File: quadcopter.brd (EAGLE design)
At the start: 178 x 178 mm, 66 parts, among them J1 ISP, SW1 PUSHBUTTON_SMD-VERTICAL-1, U2 ATMEGA128RFA1

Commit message: moved net bridge and VREG closer to battery terminals
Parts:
- moved U$2 16.7 mm to (-10.8, 9.65)
- moved J4 13.8 mm to (-16.2, 6.93), turned to 45 degrees
- moved C27 12.1 mm to (-20.4, 4.00), turned to 90 degrees
- moved C28 7.41 mm to (-30.2, 4.05), turned to 90 degrees
- moved C13 4.60 mm to (-28.1, 5.80), turned to 270 degrees
- moved STEP_DOWN 4.08 mm to (-24.6, 4.80), turned to 90 degrees
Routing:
- net 3V: track 287.6 -> 142.7 mm, vias 5 -> 9
- net RX1: track 157.3 -> 119.0 mm
- net JUMPER_INPUT: track 22.2 -> 7.57 mm
- net SCL: track 99.5 -> 87.8 mm, vias 3 -> 1
- net BAT_GND: track 109.9 -> 98.4 mm, vias 6 -> 5
- net PE4: track 125.4 -> 136.0 mm, vias 2 -> 1
- net GND: track 226.0 -> 234.1 mm, vias 30 -> 29
- net VBAT: track 41.0 -> 47.2 mm, vias 8 -> 6
- net PE5: track 108.9 -> 103.0 mm

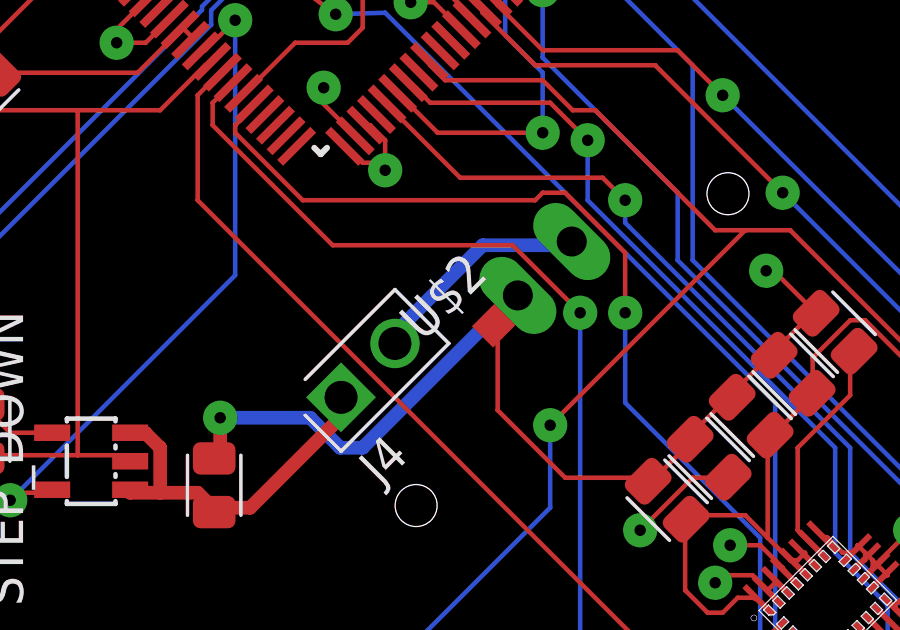
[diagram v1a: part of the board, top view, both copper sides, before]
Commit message: fixed drc things for closer net bridge
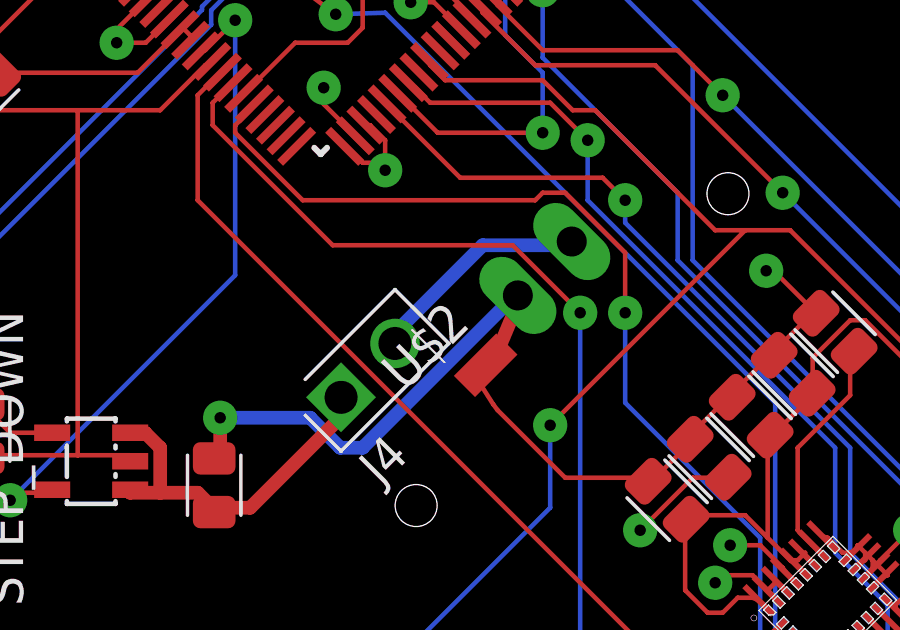
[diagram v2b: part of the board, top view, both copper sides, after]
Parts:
- moved U$2 1.76 mm to (-11.4, 8.00)
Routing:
- net BAT_GND: track 98.4 -> 100.1 mm
- net GND: track 234.1 -> 232.6 mm
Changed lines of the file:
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@@
 <attribute name="MPN" value="NA" x="-72.2" y="-0.7" size="1.778" layer="27" rot="R90" display="off"/>
 </element>
-<element name="U$2" library="quadparts_michael" package="NET_BRIDGE" value="NET_BRIDGE" x="-10.8" y="9.65" rot="R45">
-<attribute name="CREATOR" value="Michael" x="-10.8" y="9.65" size="1.778" layer="27" rot="R45" display="off"/>
-<attribute name="DIST" value="none" x="-10.8" y="9.65" size="1.778" layer="27" rot="R45" display="off"/>
-<attribute name="DISTPN" value="none" x="-10.8" y="9.65" size="1.778" layer="27" rot="R45" display="off"/>
-<attribute name="MFR" value="none" x="-10.8" y="9.65" size="1.778" layer="27" rot="R45" display="off"/>
-<attribute name="MPN" value="none" x="-10.8" y="9.65" size="1.778" layer="27" rot="R45" display="off"/>
-<attribute name="REVIEWER" value="group 4" x="-10.8" y="9.65" size="1.778" layer="27" rot="R45" display="off"/>
+<element name="U$2" library="quadparts_michael" package="NET_BRIDGE" value="NET_BRIDGE" x="-11.4" y="8" rot="R45">
+<attribute name="CREATOR" value="Michael" x="-11.4" y="8" size="1.778" layer="27" rot="R45" display="off"/>
+<attribute name="DIST" value="none" x="-11.4" y="8" size="1.778" layer="27" rot="R45" display="off"/>
+<attribute name="DISTPN" value="none" x="-11.4" y="8" size="1.778" layer="27" rot="R45" display="off"/>
+<attribute name="MFR" value="none" x="-11.4" y="8" size="1.778" layer="27" rot="R45" display="off"/>
+<attribute name="MPN" value="none" x="-11.4" y="8" size="1.778" layer="27" rot="R45" display="off"/>
+<attribute name="REVIEWER" value="group 4" x="-11.4" y="8" size="1.778" layer="27" rot="R45" display="off"/>
 </element>
 <element name="U$20" library="quadparts_michael" package="MOSFET" value="MOSFET-N_CHANNEL" x="-64.17" y="2.2">
@@
 <wire x1="-30" y1="5" x2="-30.2" y2="4.945" width="0.1524" layer="1"/>
 <wire x1="-28.25" y1="5" x2="-28.15" y2="4.905" width="0.1524" layer="1"/>
-<wire x1="-11" y1="6.5" x2="-11" y2="9.25" width="0.1524" layer="1"/>
+<wire x1="-11" y1="6.5" x2="-11.15" y2="6.7" width="0.1524" layer="1"/>
 <wire x1="-8.75" y1="4.25" x2="-11" y2="6.5" width="0.1524" layer="1"/>
 <wire x1="-6" y1="4.25" x2="-8.75" y2="4.25" width="0.1524" layer="1"/>
-<wire x1="-11" y1="9.25" x2="-11.153553125" y2="9.29644375" width="0.1524" layer="1"/>
+<wire x1="-11.15" y1="6.7" x2="-11.753553125" y2="7.64644375" width="0.1524" layer="1"/>
 <wire x1="-6" y1="4.25" x2="-5.982859375" y2="4.132859375" width="0.1524" layer="1"/>
 <wire x1="-22.25" y1="16.5" x2="-20.75" y2="18" width="0.1524" layer="1"/>
@@
 <wire x1="-20.25" y1="6.25" x2="-20.25" y2="5" width="0.4572" layer="1"/>
 <wire x1="-20.25" y1="5" x2="-20.45" y2="4.895" width="0.4572" layer="1"/>
-<wire x1="-10.25" y1="10.25" x2="-10.44644375" y2="10.003553125" width="0.4572" layer="1"/>
+<wire x1="-10.25" y1="10.25" x2="-11.04644375" y2="8.353553125" width="0.4572" layer="1"/>
 <wire x1="-10.25" y1="10.25" x2="-10.32729375" y2="10.32729375" width="0.4572" layer="1"/>
 <wire x1="-17.25" y1="6.25" x2="-20.25" y2="6.25" width="0.4572" layer="16"/>

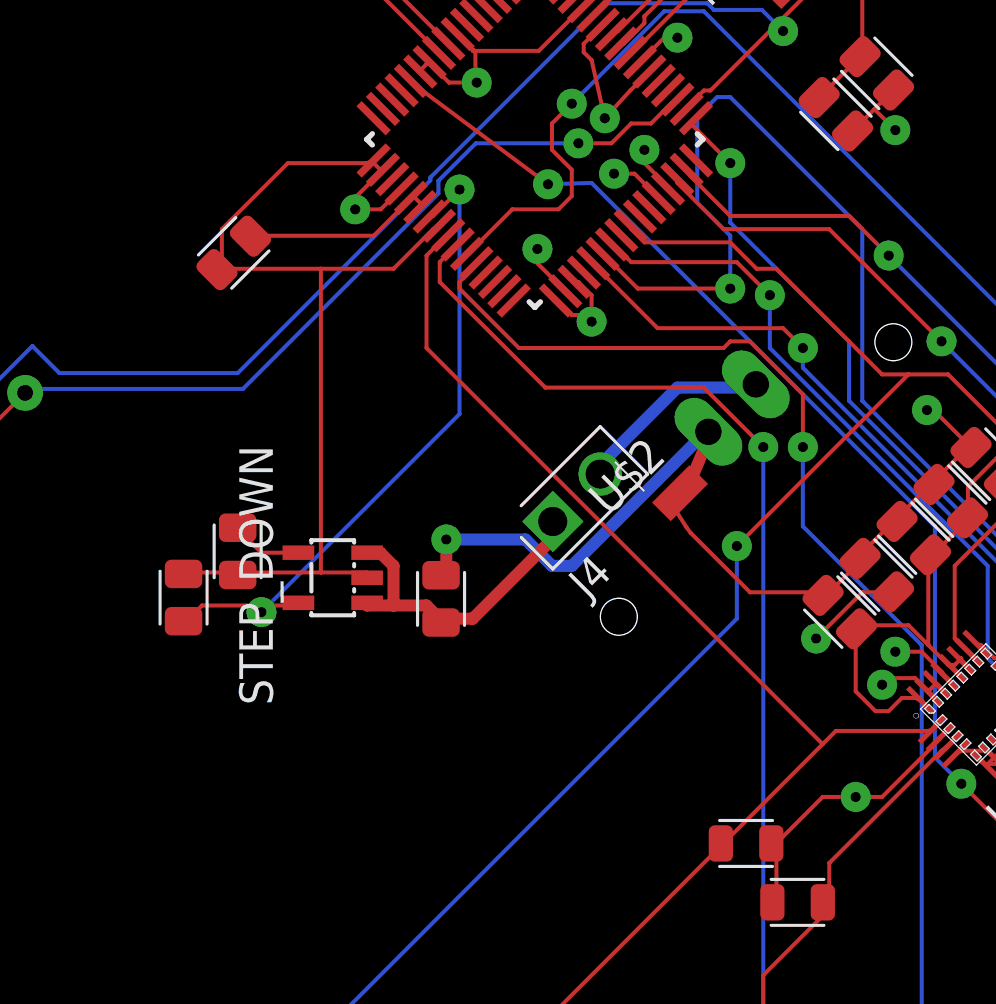
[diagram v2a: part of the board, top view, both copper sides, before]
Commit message: made vreg traces even shorter
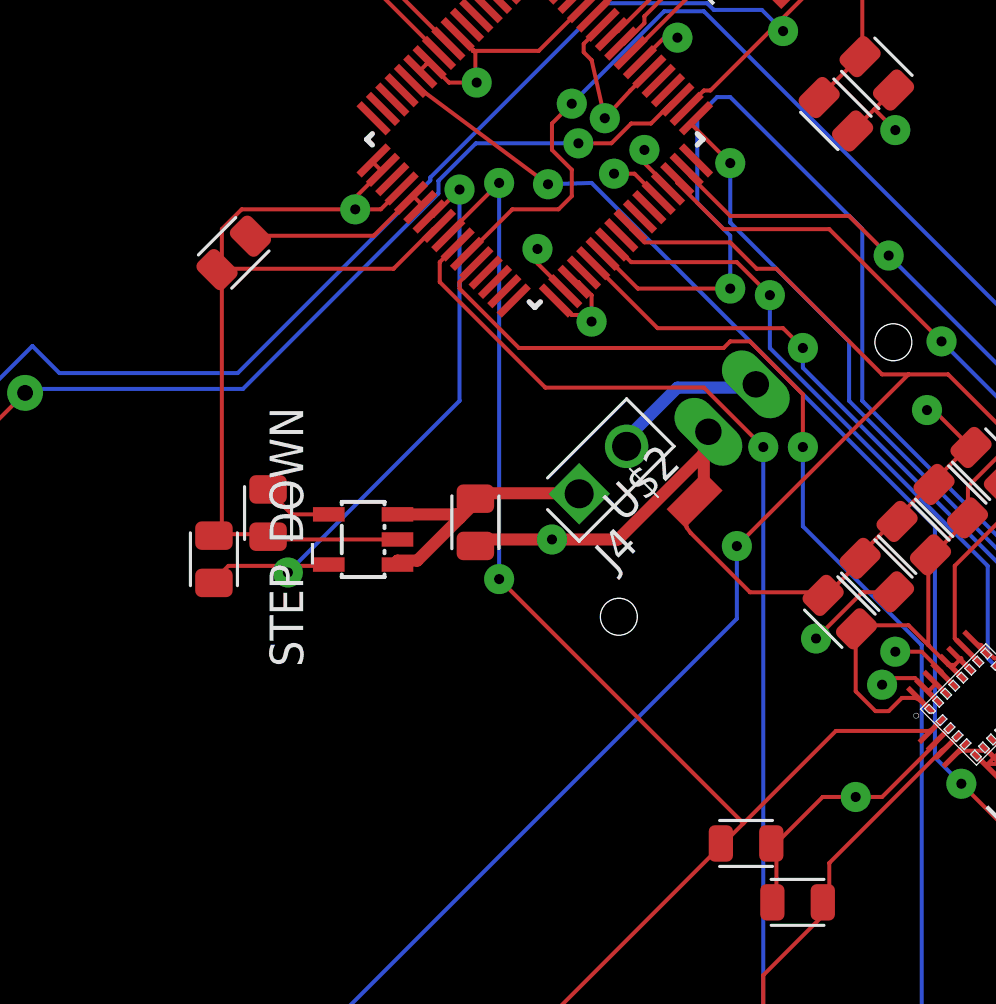
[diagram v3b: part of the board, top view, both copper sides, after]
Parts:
- moved C27 3.18 mm to (-19.1, 6.90), turned to 270 degrees
- moved STEP_DOWN 1.85 mm to (-23.4, 6.25)
- moved C13 1.85 mm to (-27.0, 7.25)
- moved C28 1.85 mm to (-29.1, 5.50)
- moved J4 1.45 mm to (-15.2, 7.98)
- moved U$2 0.60 mm to (-10.8, 7.75)
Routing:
- net SCL: track 87.8 -> 92.8 mm, vias 1 -> 3
- net GND: track 232.6 -> 229.4 mm
- net BAT_GND: track 100.1 -> 97.4 mm
- net 3V: track 142.7 -> 140.9 mm
- net JUMPER_INPUT: track 7.57 -> 6.07 mm
- net VBAT: track 47.2 -> 45.8 mm

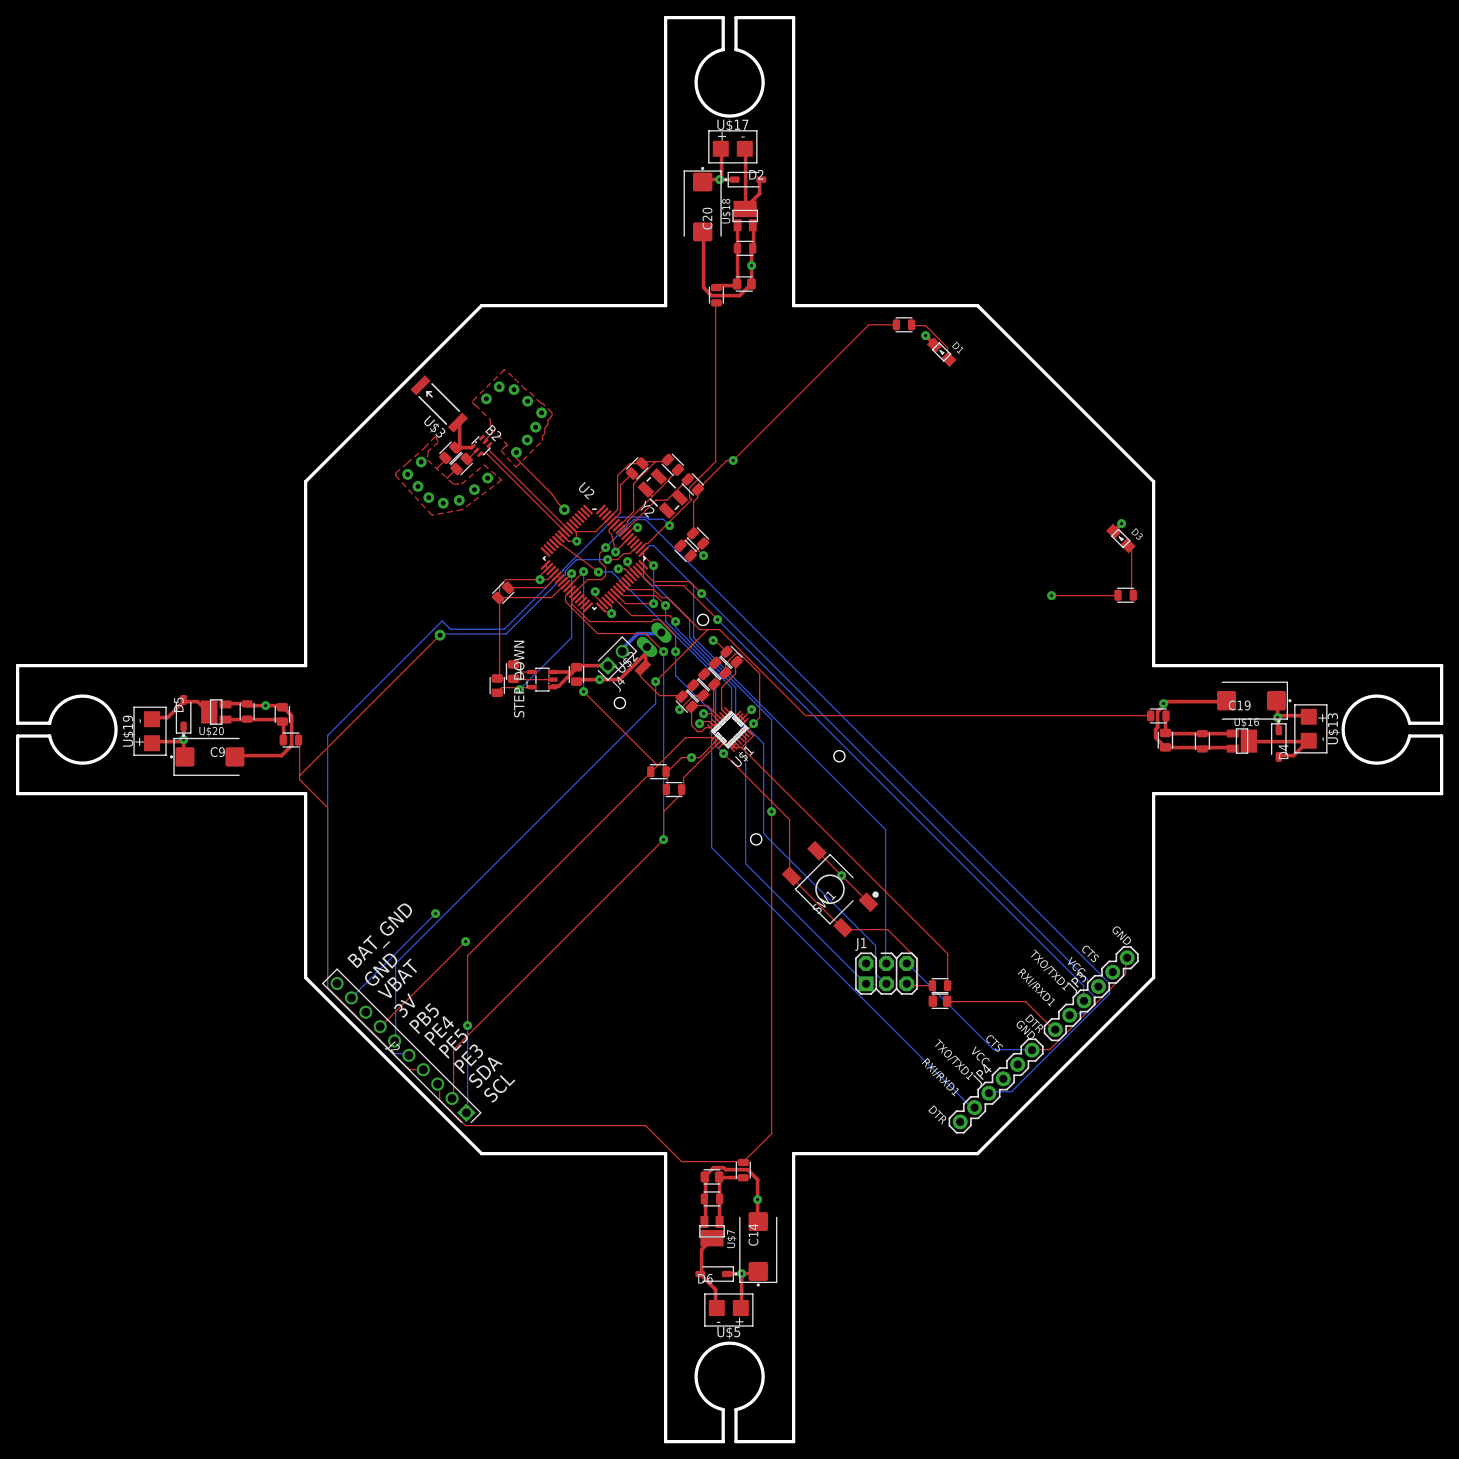
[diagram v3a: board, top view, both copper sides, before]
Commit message: rotated board to fit in box
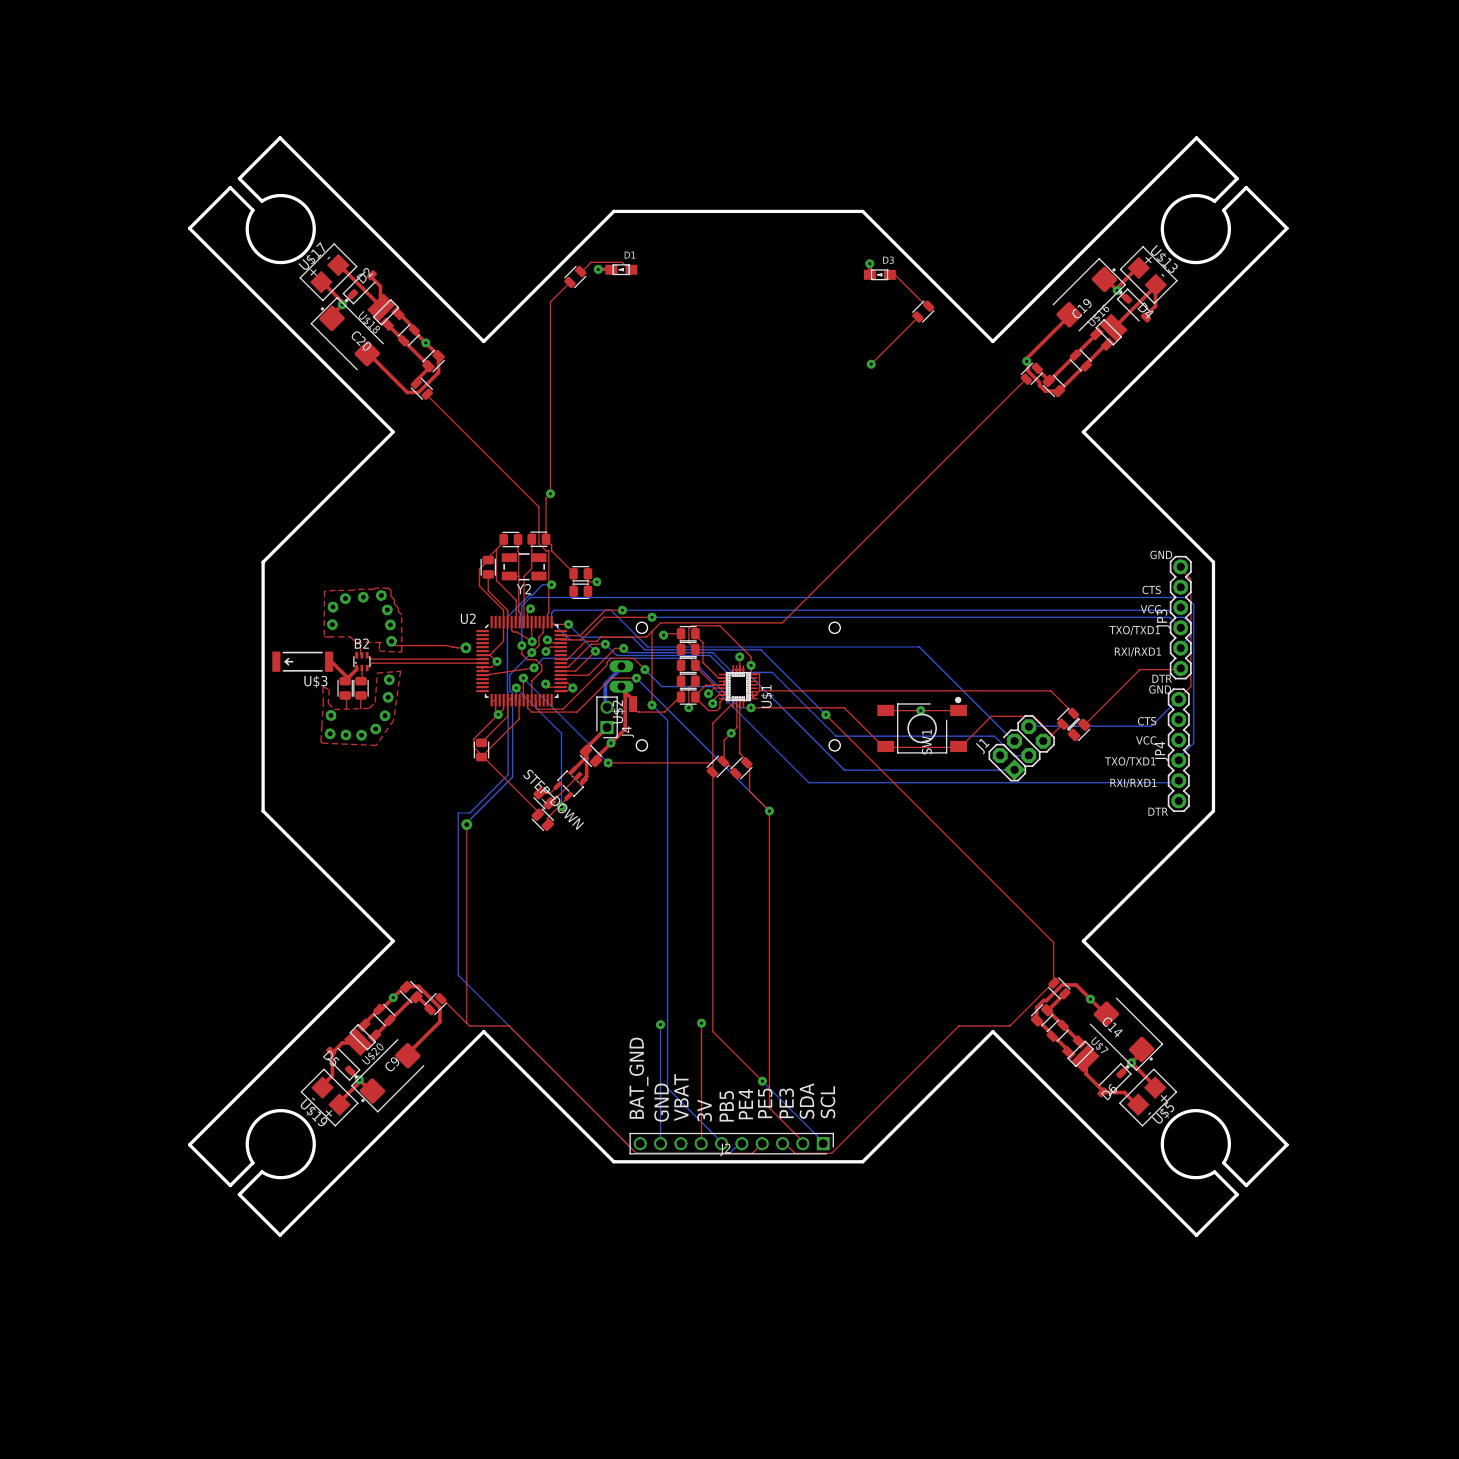
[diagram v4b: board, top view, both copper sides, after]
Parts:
- moved U$13 60.0 mm to (51.9, 57.0), turned to 315 degrees
- moved U$5 58.6 mm to (52.5, -45.5), turned to 225 degrees
- moved D4 57.3 mm to (50.9, 52.7), turned to 315 degrees
- moved D6 55.2 mm to (47.8, -44.2), turned to 225 degrees
- moved C19 54.5 mm to (44.7, 54.1), turned to 225 degrees
- moved U$16 53.7 mm to (47.4, 49.7), turned to 225 degrees
- moved C14 53.0 mm to (49.3, -37.8), turned to 135 degrees
- moved U$17 52.7 mm to (-50.3, 56.6), turned to 45 degrees
- moved U$7 51.1 mm to (43.9, -40.5), turned to 135 degrees
- moved U$19 50.8 mm to (-49.5, -46.2), turned to 135 degrees
- moved R17 50.0 mm to (43.9, 46.1), turned to 135 degrees
- moved D2 50.0 mm to (-45.9, 55.6), turned to 45 degrees
- moved JP4 48.5 mm to (56.1, -8.92), turned to 90 degrees
- moved R10 48.0 mm to (41.0, -37.7), turned to 45 degrees
- moved JP3 47.8 mm to (56.4, 7.65), turned to 90 degrees
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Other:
- board size 178 x 178 mm -> 137.2 x 137.2 mm
